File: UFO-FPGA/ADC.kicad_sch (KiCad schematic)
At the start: 0 parts

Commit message: ADC schematic met note's
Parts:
- added C45: 100n, symbol Device:C
- added C46: 10u, symbol Device:C
- added C47, C48: 470p, symbol Device:C
- added U8: ~, symbol UFO_PARTS:MAX19777AZA+T
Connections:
- new net +3V3: C45.2, C46.2, U8.A4 (Vdd)
- new net AIN1: C47.1, U8.A1 (AIN1)
- new net AIN2: C48.1, U8.A2 (AIN2)
- new net CHSEL: U8.B3 (CHSEL)
- new net GND: C45.1, C46.1, C47.2, C48.2, U8.A3 (GND)
- new net MISO: U8.B4 (DOUT)
- new net SCK: U8.B1 (SCLK)
- new net SS: U8.B2 (CS)

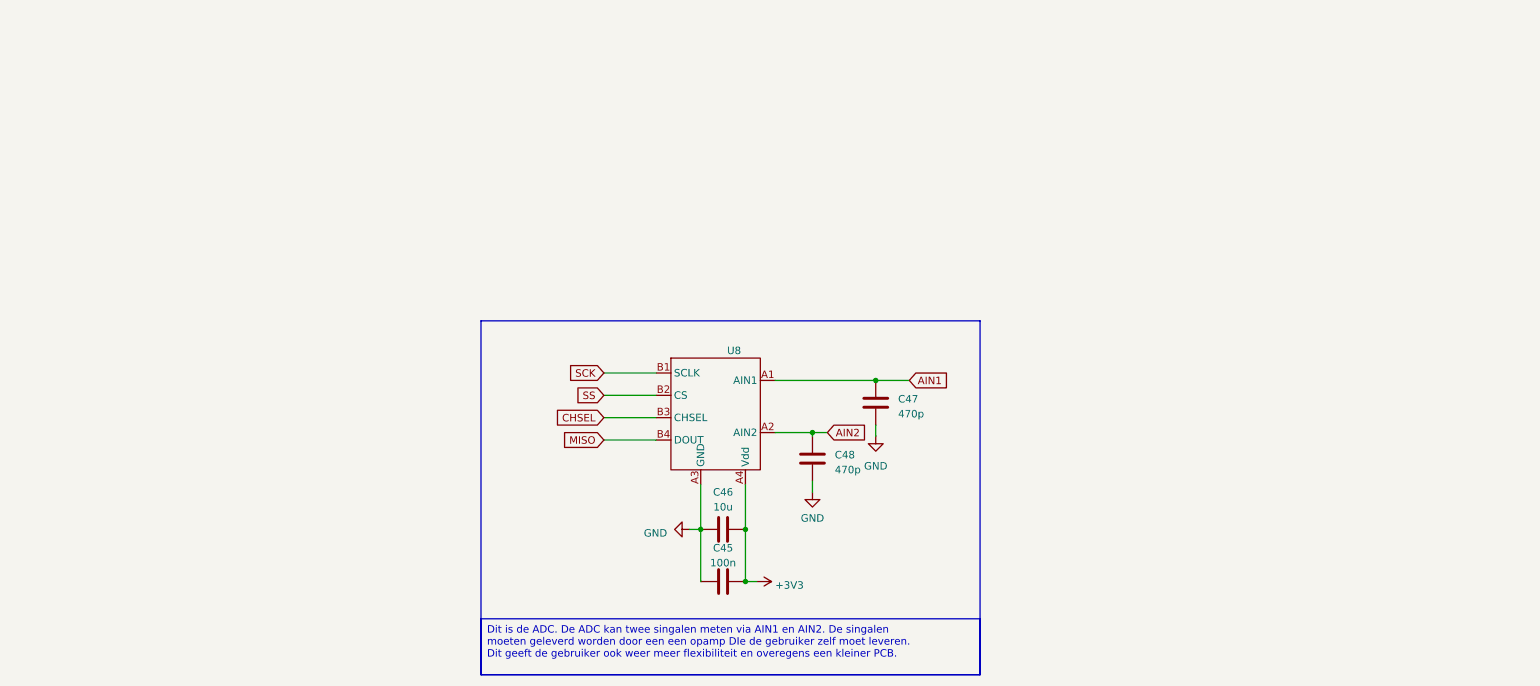
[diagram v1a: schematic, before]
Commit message: Labels and schametic changes
Updated Power schematic
Added labes for the different nets
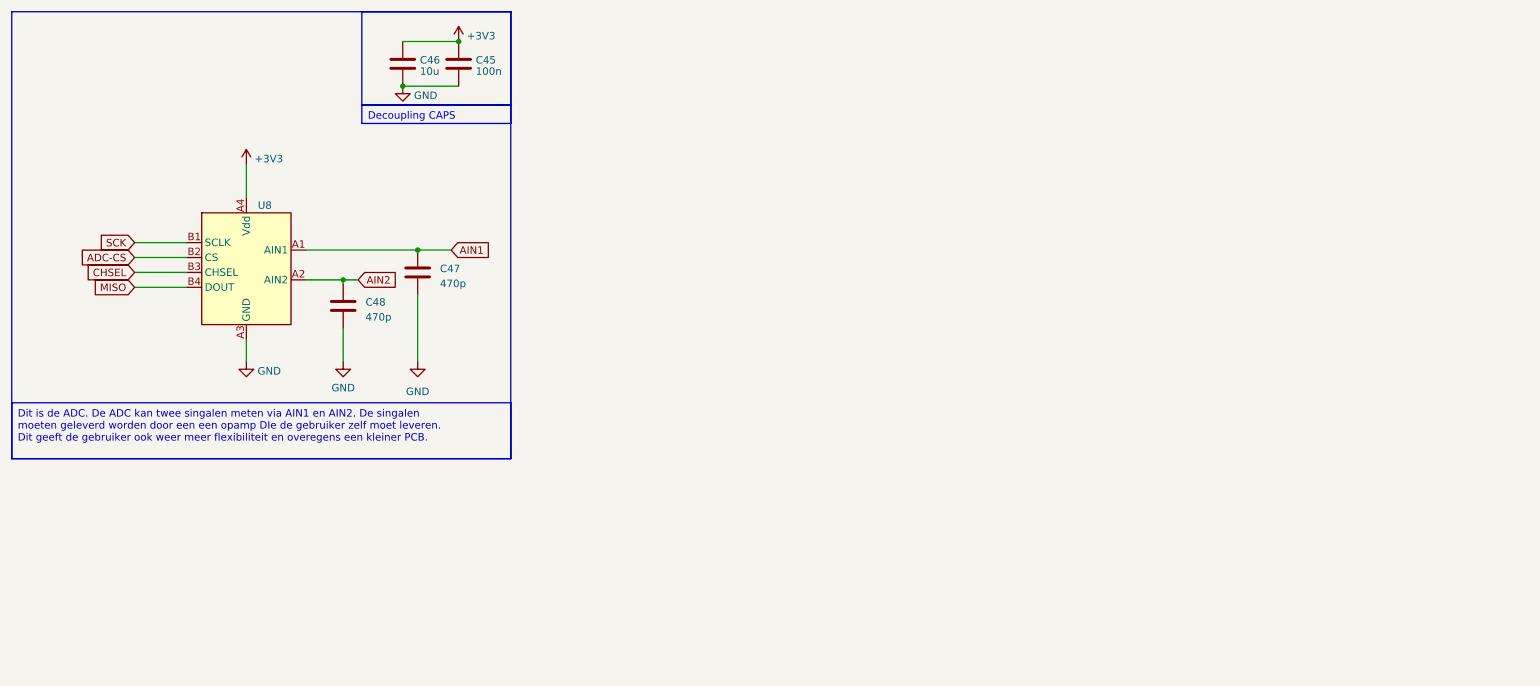
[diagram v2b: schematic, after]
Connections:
- net SS renamed ADC-CS
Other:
- moved on the sheet: C45, C46, C47, C48

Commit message: Opamp gemaakt van de ADC
Enkel nog begrijpen wat VDC is. Aan docent vragen?
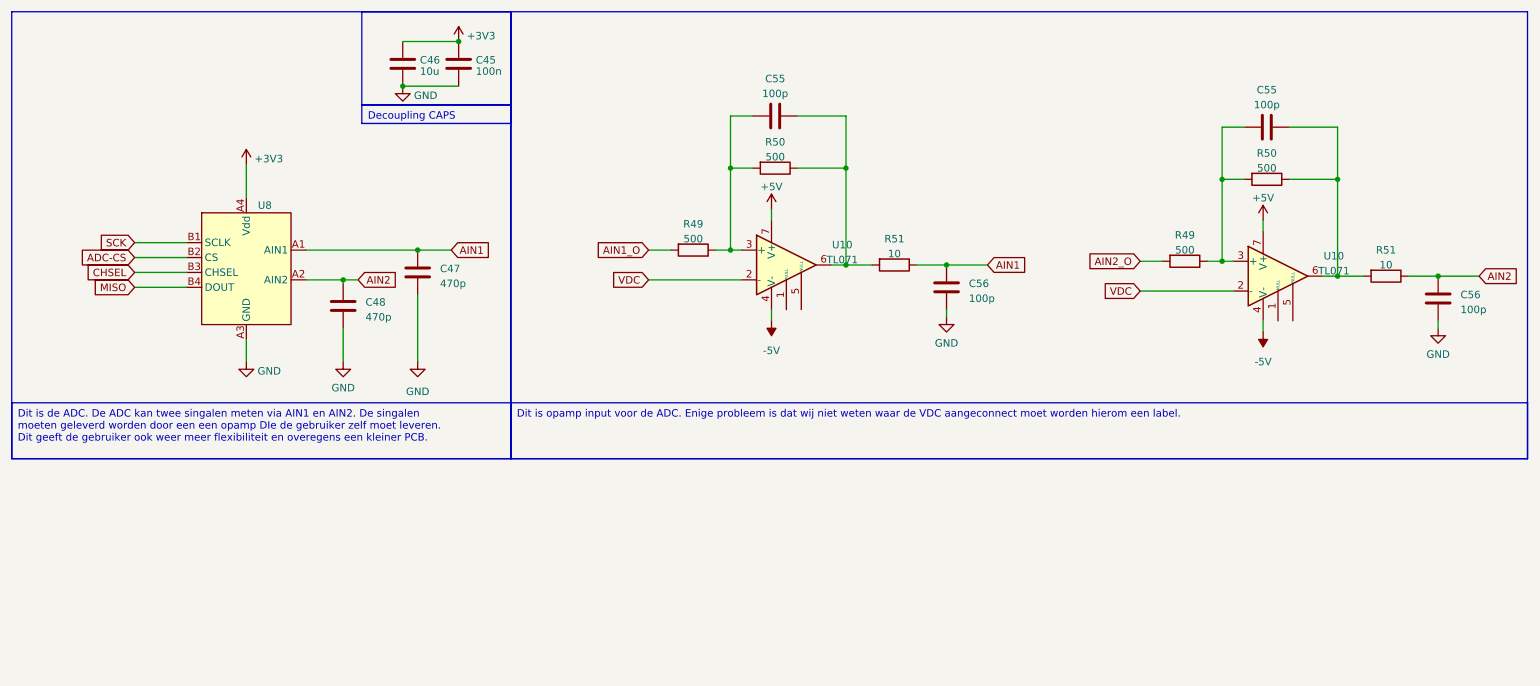
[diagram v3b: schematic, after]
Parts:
- added C55 (x2), C56 (x2): 100p, symbol Device:C
- added R49 (x2), R50 (x2): 500, symbol Device:R
- added R51 (x2): 10, symbol Device:R
- added U10 (x2): TL071, symbol Amplifier_Operational:TL071
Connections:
- net AIN1: now also C56.2, R51.1
- net AIN2: now also C56.2, R51.1
- net GND: now also C56.1, C56.1
- new net: C55.2, R50.1, R51.2, U10.6 (x2)
- new net: C55.1, R49.1, R50.2, U10.3 (+) (x2)
- new net +5V: U10.7 (V+), U10.7 (V+)
- new net -5V: U10.4 (V-), U10.4 (V-)
- new net AIN1_O: R49.2
- new net AIN2_O: R49.2
- new net VDC: U10.2 (-), U10.2 (-)

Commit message: Revision
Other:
- company: (none) -> Universal-Field-Objects
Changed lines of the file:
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@@
 (kicad_sch (version 20230121) (generator eeschema)
   (paper "A4")
+  (title_block
+    (date "2023-04-25")
+    (rev "V0.5")
+    (company "Universal-Field-Objects")
+  )
   (junction (at 141.605 59.055) (diameter 0) (color 0 0 0 0)
   )

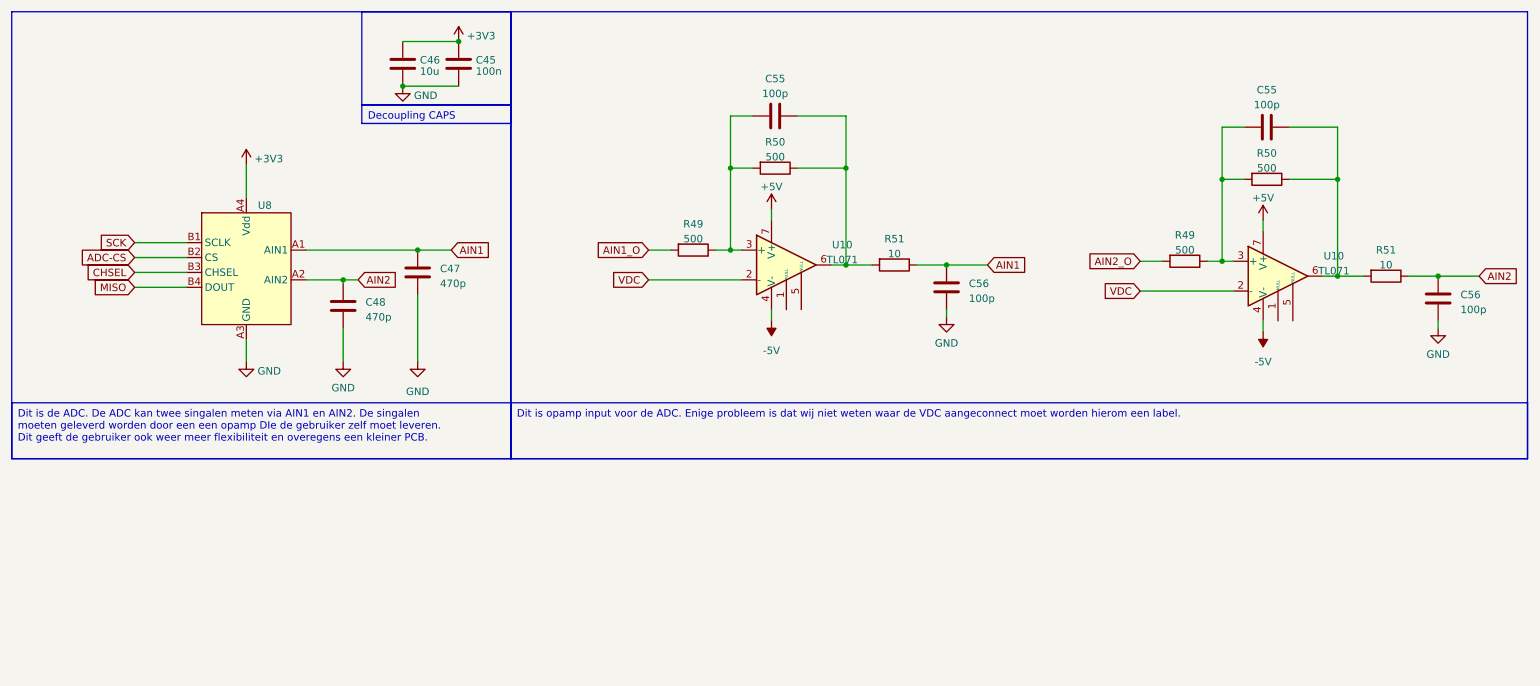
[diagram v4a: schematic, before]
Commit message: PCB and footprint
Added foorprints and moved on pcb layout
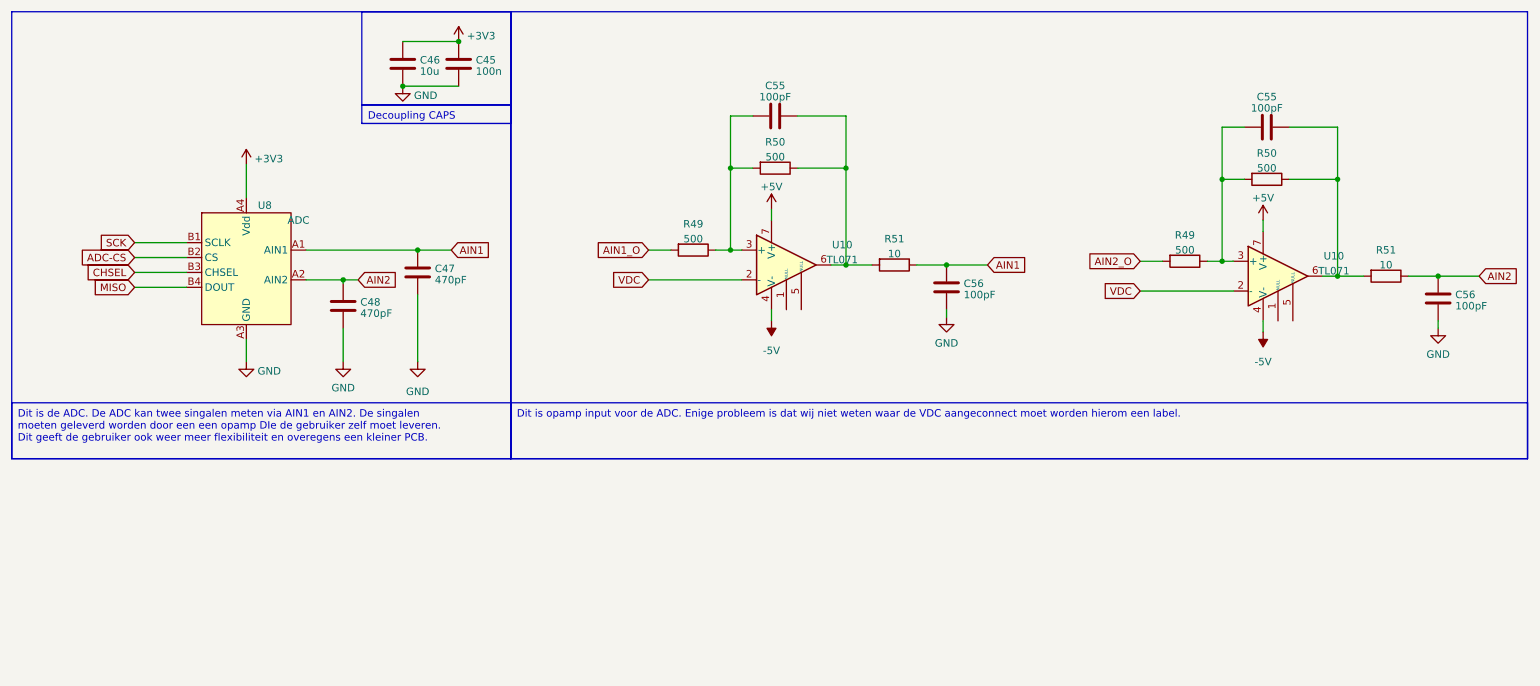
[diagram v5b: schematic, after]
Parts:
- C47, C48: value 470p -> 470pF
- C55, C56: value 100p -> 100pF
- U10: footprint (none) -> Package_TO_SOT_SMD:SOT-23-5_HandSoldering
- U8: value ~ -> ADC; footprint (none) -> UFO-Footpints:WLP-8
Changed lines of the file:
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@@
   (symbol (lib_id "Device:C") (at 149.225 36.195 90) (unit 1)
     (in_bom yes) (on_board yes) (dnp no) (fields_autoplaced)
-    (property "Reference" "C55" (at 149.225 29.845 90)
-      (effects (font (size 1.27 1.27)))
-    )
-    (property "Value" "100p" (at 149.225 32.385 90)
+    (property "Reference" "C55" (at 149.225 31.0261 90)
+      (effects (font (size 1.27 1.27)))
+    )
+    (property "Value" "100pF" (at 149.225 32.9471 90)
       (effects (font (size 1.27 1.27)))
     )
@@
   (symbol (lib_id "Device:C") (at 75.565 68.58 0) (unit 1)
     (in_bom yes) (on_board yes) (dnp no) (fields_autoplaced)
-    (property "Reference" "C48" (at 79.375 67.945 0)
-      (effects (font (size 1.27 1.27)) (justify left))
-    )
-    (property "Value" "470p" (at 79.375 70.485 0)
+    (property "Reference" "C48" (at 78.486 67.9363 0)
+      (effects (font (size 1.27 1.27)) (justify left))
+    )
+    (property "Value" "470pF" (at 78.486 69.8573 0)
       (effects (font (size 1.27 1.27)) (justify left))
     )
@@
       (effects (font (size 1.27 1.27)) (justify left))
     )
-    (property "Value" "~" (at 67.945 53.975 0)
-      (effects (font (size 1.27 1.27)))
-    )
-    (property "Footprint" "" (at 67.945 53.975 0)
+    (property "Value" "ADC" (at 67.945 53.975 0)
+      (effects (font (size 1.27 1.27)))
+    )
+    (property "Footprint" "UFO-Footpints:WLP-8" (at 73.025 76.835 0)
       (effects (font (size 1.27 1.27)) hide)
     )
@@
       (effects (font (size 1.27 1.27)))
     )
-    (property "Footprint" "" (at 236.22 62.23 0)
+    (property "Footprint" "Package_TO_SOT_SMD:SOT-23-5_HandSoldering" (at 236.22 62.23 0)
       (effects (font (size 1.27 1.27)) hide)
     )
@@
   (symbol (lib_id "Device:C") (at 233.045 38.1 90) (unit 1)
     (in_bom yes) (on_board yes) (dnp no) (fields_autoplaced)
-    (property "Reference" "C55" (at 233.045 31.75 90)
-      (effects (font (size 1.27 1.27)))
-    )
-    (property "Value" "100p" (at 233.045 34.29 90)
+    (property "Reference" "C55" (at 233.045 32.9311 90)
+      (effects (font (size 1.27 1.27)))
+    )
+    (property "Value" "100pF" (at 233.045 34.8521 90)
       (effects (font (size 1.27 1.27)))
     )
@@
   (symbol (lib_id "Device:C") (at 262.255 67.31 180) (unit 1)
     (in_bom yes) (on_board yes) (dnp no) (fields_autoplaced)
-    (property "Reference" "C56" (at 266.065 66.675 0)
+    (property "Reference" "C56" (at 265.176 66.6663 0)
       (effects (font (size 1.27 1.27)) (justify right))
     )
-    (property "Value" "100p" (at 266.065 69.215 0)
+    (property "Value" "100pF" (at 265.176 68.5873 0)
       (effects (font (size 1.27 1.27)) (justify right))
     )
@@
   (symbol (lib_id "Device:C") (at 88.265 62.865 0) (unit 1)
     (in_bom yes) (on_board yes) (dnp no) (fields_autoplaced)
-    (property "Reference" "C47" (at 92.075 62.23 0)
-      (effects (font (size 1.27 1.27)) (justify left))
-    )
-    (property "Value" "470p" (at 92.075 64.77 0)
+    (property "Reference" "C47" (at 91.186 62.2213 0)
+      (effects (font (size 1.27 1.27)) (justify left))
+    )
+    (property "Value" "470pF" (at 91.186 64.1423 0)
       (effects (font (size 1.27 1.27)) (justify left))
     )
@@
   (symbol (lib_id "Device:C") (at 178.435 65.405 180) (unit 1)
     (in_bom yes) (on_board yes) (dnp no) (fields_autoplaced)
-    (property "Reference" "C56" (at 182.245 64.77 0)
+    (property "Reference" "C56" (at 181.356 64.7613 0)
       (effects (font (size 1.27 1.27)) (justify right))
     )
-    (property "Value" "100p" (at 182.245 67.31 0)
+    (property "Value" "100pF" (at 181.356 66.6823 0)
       (effects (font (size 1.27 1.27)) (justify right))
     )
@@
       (effects (font (size 1.27 1.27)))
     )
-    (property "Footprint" "" (at 152.4 60.325 0)
-      (effects (font (size 1.27 1.27)) hide)
-    )
+    (property "Footprint" "Package_TO_SOT_SMD:SOT-23-5_HandSoldering" (at 152.4 60.325 0)
+      (effects (font (size 1.27 1.27)) hide)
+    )

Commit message: Schakeling ADC gemaakt 1 opamp weg gehaald
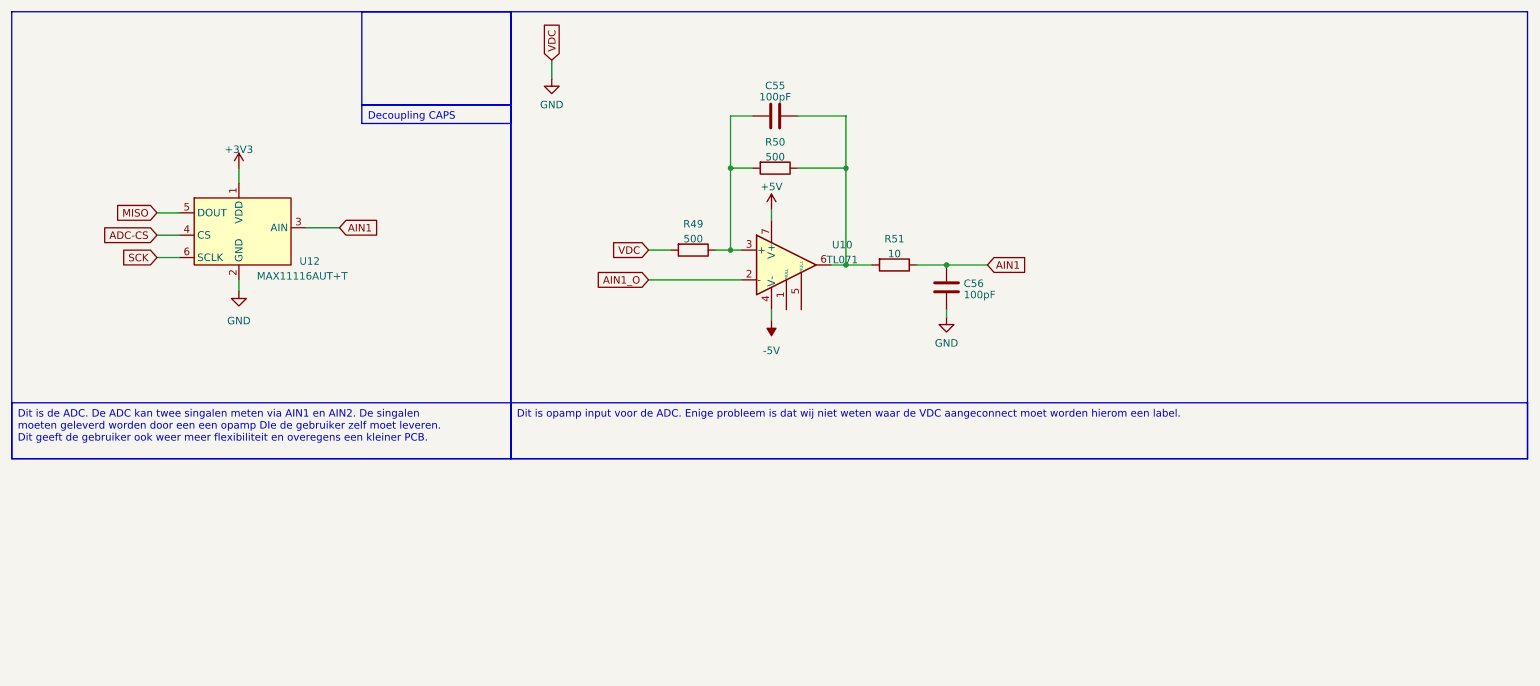
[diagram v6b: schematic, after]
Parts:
- removed C45: 100n, symbol Device:C
- removed C46: 10u, symbol Device:C
- removed C47, C48: 470pF, symbol Device:C
- removed C55, C56: 100pF, symbol Device:C
- removed R49, R50: 500, symbol Device:R
- removed R51: 10, symbol Device:R
- removed U10: TL071, Package_TO_SOT_SMD:SOT-23-5_HandSoldering, symbol Amplifier_Operational:TL071
- removed U8: ADC, UFO-Footpints:WLP-8, symbol UFO_PARTS:MAX19777AZA+T
- added U12: MAX11116AUT+T, Package_TO_SOT_SMD:SOT-23-6_Handsoldering, symbol UFO_PARTS:MAX11116AUT+T
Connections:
- net VDC is gone; now on net AIN1_O: U10.2 (-)
- net +3V3: now also U12.1 (VDD)
- net ADC-CS: now also U12.4 (CS)
- net AIN1: now also U12.3 (AIN)
- net AIN1_O: no longer R49.2
- net GND: now also R49.2, U12.2 (GND)
- net MISO: now also U12.5 (DOUT)
- net SCK: now also U12.6 (SCLK)

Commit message: footprint
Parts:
- C55, C56: footprint (none) -> Capacitor_SMD:C_0805_2012Metric_Pad1.18x1.45mm_HandSolder
- R49, R50, R51: footprint (none) -> Resistor_SMD:R_0805_2012Metric
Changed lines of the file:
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@@
       (effects (font (size 1.27 1.27)))
     )
-    (property "Footprint" "" (at 153.035 35.2298 0)
+    (property "Footprint" "Capacitor_SMD:C_0805_2012Metric_Pad1.18x1.45mm_HandSolder" (at 153.035 35.2298 0)
       (effects (font (size 1.27 1.27)) hide)
     )
@@
       (effects (font (size 1.27 1.27)))
     )
-    (property "Footprint" "" (at 135.255 57.277 90)
+    (property "Footprint" "Resistor_SMD:R_0805_2012Metric" (at 135.255 57.277 90)
       (effects (font (size 1.27 1.27)) hide)
     )
@@
       (effects (font (size 1.27 1.27)))
     )
-    (property "Footprint" "" (at 149.225 43.307 90)
+    (property "Footprint" "Resistor_SMD:R_0805_2012Metric" (at 149.225 43.307 90)
       (effects (font (size 1.27 1.27)) hide)
     )
@@
       (effects (font (size 1.27 1.27)))
     )
-    (property "Footprint" "" (at 169.545 59.817 90)
+    (property "Footprint" "Resistor_SMD:R_0805_2012Metric" (at 169.545 59.817 90)
       (effects (font (size 1.27 1.27)) hide)
     )
@@
       (effects (font (size 1.27 1.27)) (justify right))
     )
-    (property "Footprint" "" (at 177.4698 61.595 0)
-      (effects (font (size 1.27 1.27)) hide)
-    )
+    (property "Footprint" "Capacitor_SMD:C_0805_2012Metric_Pad1.18x1.45mm_HandSolder" (at 177.4698 61.595 0)
+      (effects (font (size 1.27 1.27)) hide)
+    )

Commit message: Footprints and values
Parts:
- R49, R50: value 500 -> 510
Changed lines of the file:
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@@
       (effects (font (size 1.27 1.27)))
     )
-    (property "Value" "500" (at 135.255 57.15 90)
+    (property "Value" "510" (at 135.255 57.15 90)
       (effects (font (size 1.27 1.27)))
     )
@@
   (symbol (lib_id "Device:R") (at 149.225 45.085 270) (unit 1)
     (in_bom yes) (on_board yes) (dnp no) (fields_autoplaced)
-    (property "Reference" "R50" (at 149.225 40.64 90)
+    (property "Reference" "R50" (at 149.225 41.0591 90)
       (effects (font (size 1.27 1.27)))
     )
-    (property "Value" "500" (at 149.225 43.18 90)
+    (property "Value" "510" (at 149.225 42.9801 90)
       (effects (font (size 1.27 1.27)))
     )
